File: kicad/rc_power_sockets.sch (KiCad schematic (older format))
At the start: 27 parts, among them IC1 ATTINY85, J1 PIR, J2 433MHZ, J3 433MHZ, P1 ICSP, Q1 NMOS, Q2 PMOS, U1 NCP4624DSN33T1G

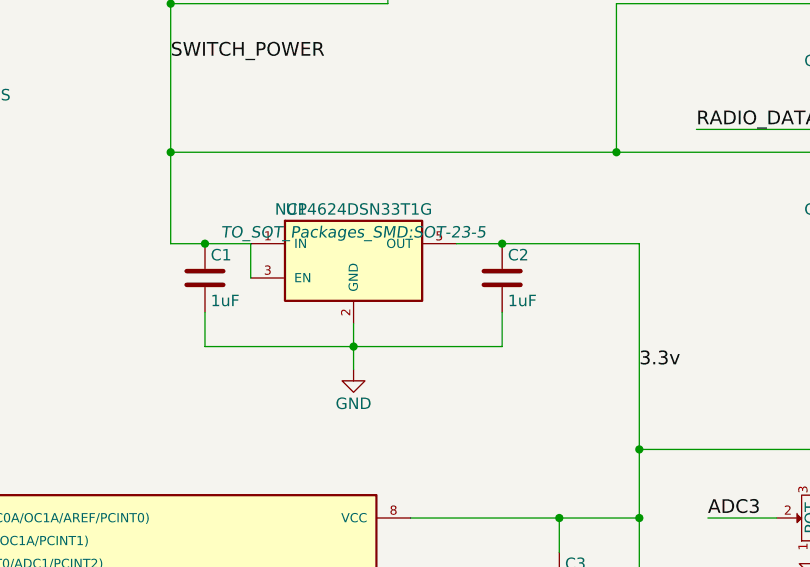
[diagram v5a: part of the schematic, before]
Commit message: MCP1755S 3v3 voltage regulator
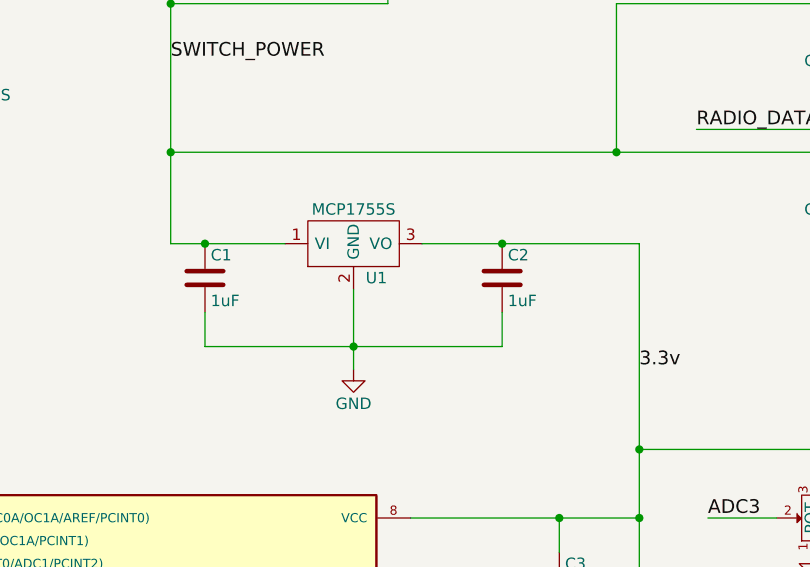
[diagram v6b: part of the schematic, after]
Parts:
- removed U1: NCP4624DSN33T1G, TO_SOT_Packages_SMD:SOT-23-5, symbol TLV70012DDC
- added U1: MCP1755S, TO_SOT_Packages_SMD:SOT-223, symbol MCP1754ST-3302E/MB
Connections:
- net 3.3v: now also U1.3 (VO)
- net GND: now also U1.2 (GND)
- net SWITCH_POWER: now also U1.1 (VI)
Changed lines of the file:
@@
 Connection ~ 5550 2450
 Wire Wire Line
-	6550 3850 6900 3850
+	6550 3850 7050 3850
 Connection ~ 6700 3850
 Wire Wire Line
-	7800 3850 8600 3850
-Wire Wire Line
-	7350 4200 7350 4400
+	7650 3850 8600 3850
+Wire Wire Line
+	7350 4050 7350 4400
 Wire Wire Line
 	6700 4150 6700 4300
@@
 	0    -1   -1   0
 $EndComp
-$Comp
-L TLV70012DDC U1
-U 1 1 56F2FC5E
-P 7350 3900
-F 0 "U1" H 7100 4100 50  0000 C CNN
-F 1 "NCP4624DSN33T1G" H 7350 4100 50  0000 C CNN
-F 2 "TO_SOT_Packages_SMD:SOT-23-5" H 7350 4000 50  0000 C CIN
-F 3 "" H 7350 3900 50  0000 C CNN
-	1    7350 3900
-	1    0    0    -1
-$EndComp
-Wire Wire Line
-	6900 3850 6900 4000
 Wire Wire Line
 	4100 5550 4900 5550
@@
 Text Label 5700 950  0    60   ~ 0
 VCC
+$Comp
+L MCP1754ST-3302E/MB U1
+U 1 1 56F6D198
+P 7350 3850
+F 0 "U1" H 7450 3700 50  0000 C CNN
+F 1 "MCP1755S" H 7350 4000 50  0000 C CNN
+F 2 "TO_SOT_Packages_SMD:SOT-223" H 7350 3850 50  0001 C CNN
+F 3 "" H 7350 3850 50  0000 C CNN
+	1    7350 3850
+	1    0    0    -1
+$EndComp
 $EndSCHEMATC

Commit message: Ground the 4th pin of the regulator
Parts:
- removed U1: MCP1755S, TO_SOT_Packages_SMD:SOT-223, symbol MCP1754ST-3302E/MB
- added U1: MCP1755ST-3302E/DB, TO_SOT_Packages_SMD:SOT-223, symbol MCP1755ST-3302E/DB
- R2, R3, R4: value 100K -> 10K
- R5: value 220 -> 820
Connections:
- net 3.3v: now also U1.3 (VO)
- net GND: now also U1.2 (GND), U1.4 (GND)
- net SWITCH_POWER: now also U1.1 (VI)
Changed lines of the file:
@@
 P 5550 2250
 F 0 "R2" V 5630 2250 50  0000 C CNN
-F 1 "100K" V 5550 2250 50  0000 C CNN
+F 1 "10K" V 5550 2250 50  0000 C CNN
 F 2 "Resistors_SMD:R_0805_HandSoldering" V 5480 2250 50  0001 C CNN
 F 3 "" H 5550 2250 50  0000 C CNN
@@
 P 5150 3500
 F 0 "R3" V 5230 3500 50  0000 C CNN
-F 1 "100K" V 5150 3500 50  0000 C CNN
+F 1 "10K" V 5150 3500 50  0000 C CNN
 F 2 "Resistors_SMD:R_0805_HandSoldering" V 5080 3500 50  0001 C CNN
 F 3 "" H 5150 3500 50  0000 C CNN
@@
 P 4100 5700
 F 0 "R4" V 4180 5700 50  0000 C CNN
-F 1 "100K" V 4100 5700 50  0000 C CNN
+F 1 "10K" V 4100 5700 50  0000 C CNN
 F 2 "Resistors_SMD:R_0805_HandSoldering" V 4030 5700 50  0001 C CNN
 F 3 "" H 4100 5700 50  0000 C CNN
@@
 P 2300 5050
 F 0 "R5" V 2380 5050 50  0000 C CNN
-F 1 "220" V 2300 5050 50  0000 C CNN
+F 1 "820" V 2300 5050 50  0000 C CNN
 F 2 "Resistors_SMD:R_0805_HandSoldering" V 2230 5050 50  0001 C CNN
 F 3 "" H 2300 5050 50  0000 C CNN
@@
 VCC
 $Comp
-L MCP1754ST-3302E/MB U1
-U 1 1 56F6D198
+L MCP1755ST-3302E/DB U1
+U 1 1 56F7151A
 P 7350 3850
-F 0 "U1" H 7450 3700 50  0000 C CNN
-F 1 "MCP1755S" H 7350 4000 50  0000 C CNN
+F 0 "U1" H 7500 3700 50  0000 C CNN
+F 1 "MCP1755ST-3302E/DB" H 7350 4000 50  0000 C CNN
 F 2 "TO_SOT_Packages_SMD:SOT-223" H 7350 3850 50  0001 C CNN
 F 3 "" H 7350 3850 50  0000 C CNN
@@
 	1    0    0    -1
 $EndComp
+Wire Wire Line
+	7300 4050 7400 4050
+Connection ~ 7350 4050
 $EndSCHEMATC

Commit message: Ground tidy
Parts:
- BT1, BT2: footprint Connect:CR2032H -> theapi_footprints:CR2032H
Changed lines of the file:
@@
 F 0 "BT1" H 6150 1150 50  0000 L CNN
 F 1 "Battery" H 6150 1050 50  0000 L CNN
-F 2 "Connect:CR2032H" V 6050 1140 50  0001 C CNN
+F 2 "theapi_footprints:CR2032H" V 6050 1140 50  0001 C CNN
 F 3 "" V 6050 1140 50  0000 C CNN
 	1    6050 1100
@@
 F 0 "BT2" H 6150 1550 50  0000 L CNN
 F 1 "Battery" H 6150 1450 50  0000 L CNN
-F 2 "Connect:CR2032H" V 6050 1540 50  0001 C CNN
+F 2 "theapi_footprints:CR2032H" V 6050 1540 50  0001 C CNN
 F 3 "" V 6050 1540 50  0000 C CNN
 	1    6050 1500
